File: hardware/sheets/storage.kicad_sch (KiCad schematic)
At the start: 32 parts, among them J1 Conn_02x20_Odd_Even, J2 Conn_02x25_Odd_Even, Q1 2N7002, U1 74HC04, U10 74LVC573A, U11 74HC138, U2 74HC08, U3 74HC08, U4 74HC32, U5 74LVC125A, U6 74HC138, U7 74HC138, U8 74LVC245A, U9 74LVC573A

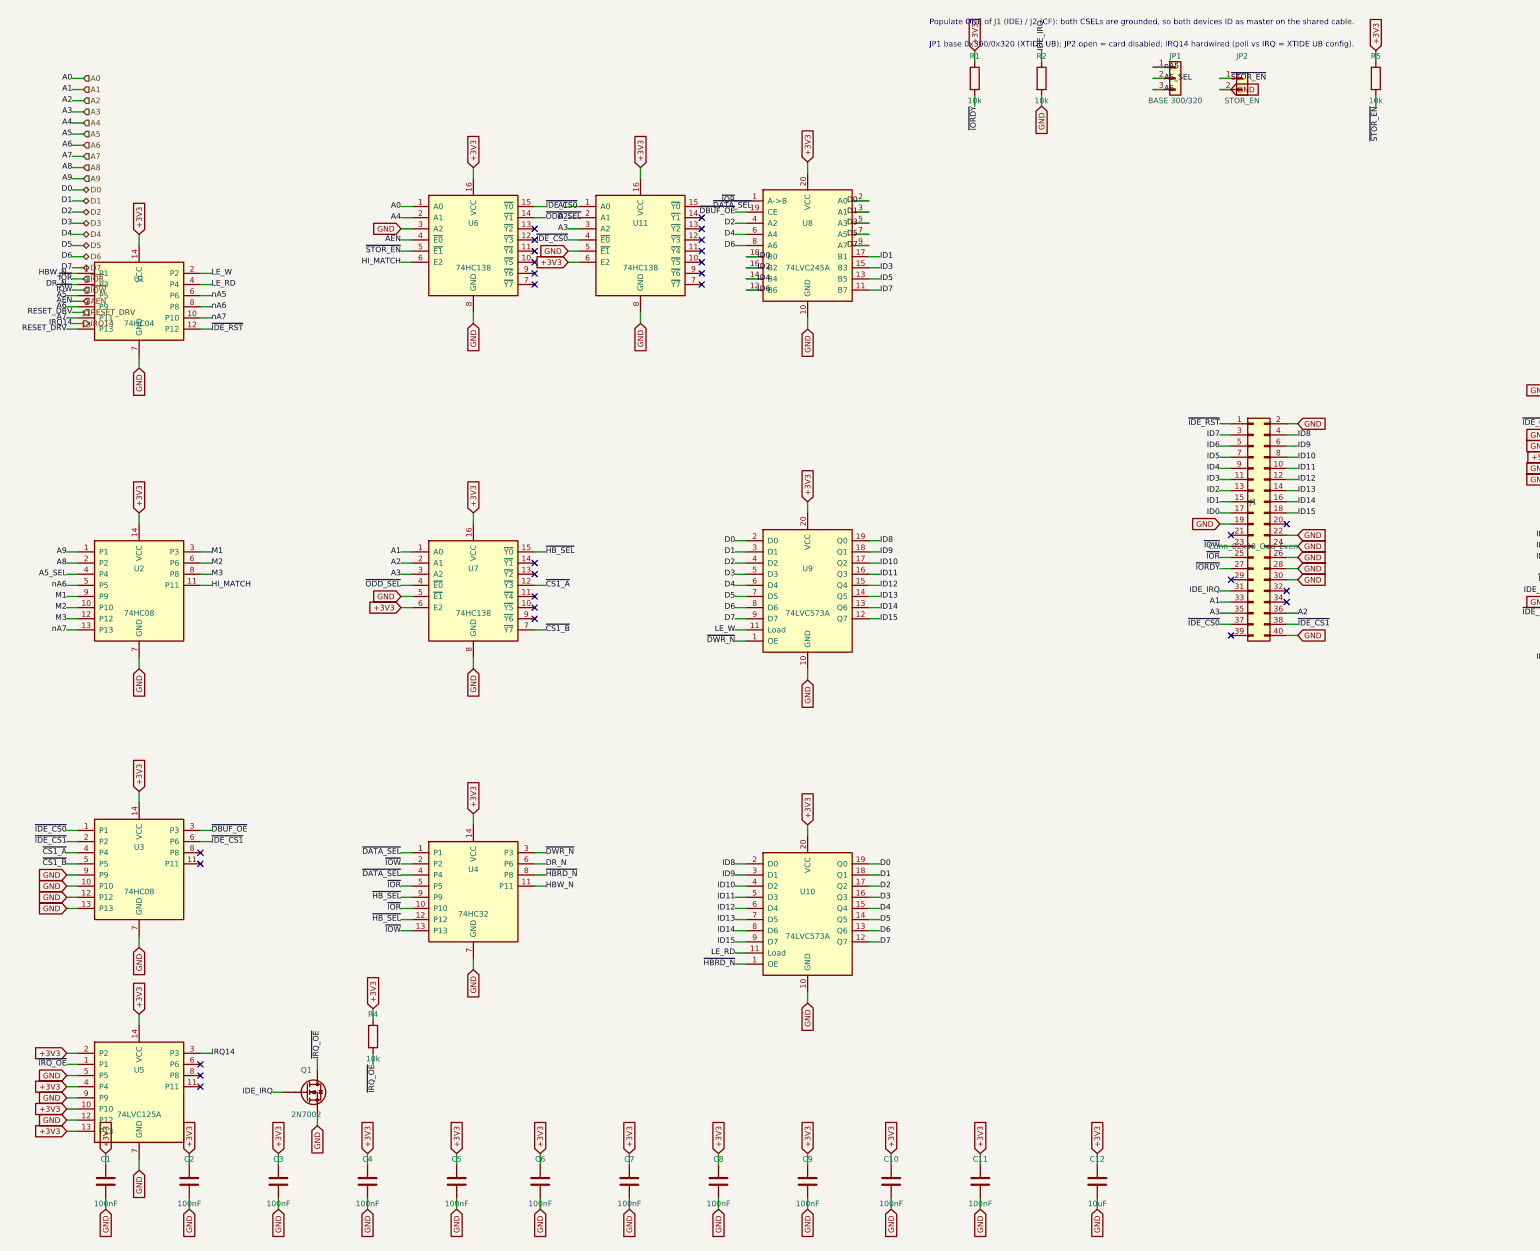
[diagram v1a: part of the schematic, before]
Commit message: addr_decode: central I/O decode, IRQ mapping + disable jumpers; UART -> TL16C550CPFBR
New addr_decode sheet owns the discrete peripherals' bus plumbing:
'138+'00+'32 windowed decode exports ~COM1/~COM2/~LPT/~IDE chip selects
(0x3F8/0x2F8/0x378 share one A5.A4.A3 fine term); one shared 74LVC125A
maps the peripherals' private IRQ requests onto IRQ4/3/7/14 (COM keeps
~OUT2 gating), replacing the three per-sheet '125s; base straps (JP1/JP2,
pulled-high commons) and per-peripheral disable jumpers JP3-JP6 (enabled
by default, fit to disable via a second '32 rank on the CS) live here.
com_port/parallel/storage lose their decode gates, IRQ drivers and
enable jumpers; board drops 97 -> 93 ICs. Docs reframed per feedback:
PRIV_CS/PRIV_IRQREQ are shared logic factored out, not isolation breaks.

UART rebound to the active TL16C550CPFBR (TQFP-48, LCSC C882798, thin
stock) -- pinout verified identical to the symbol via jlc_get_pinout;
parts.py-only swap, sourcing notes updated.

Co-Authored-By: Claude Fable 5 <noreply@anthropic.com>
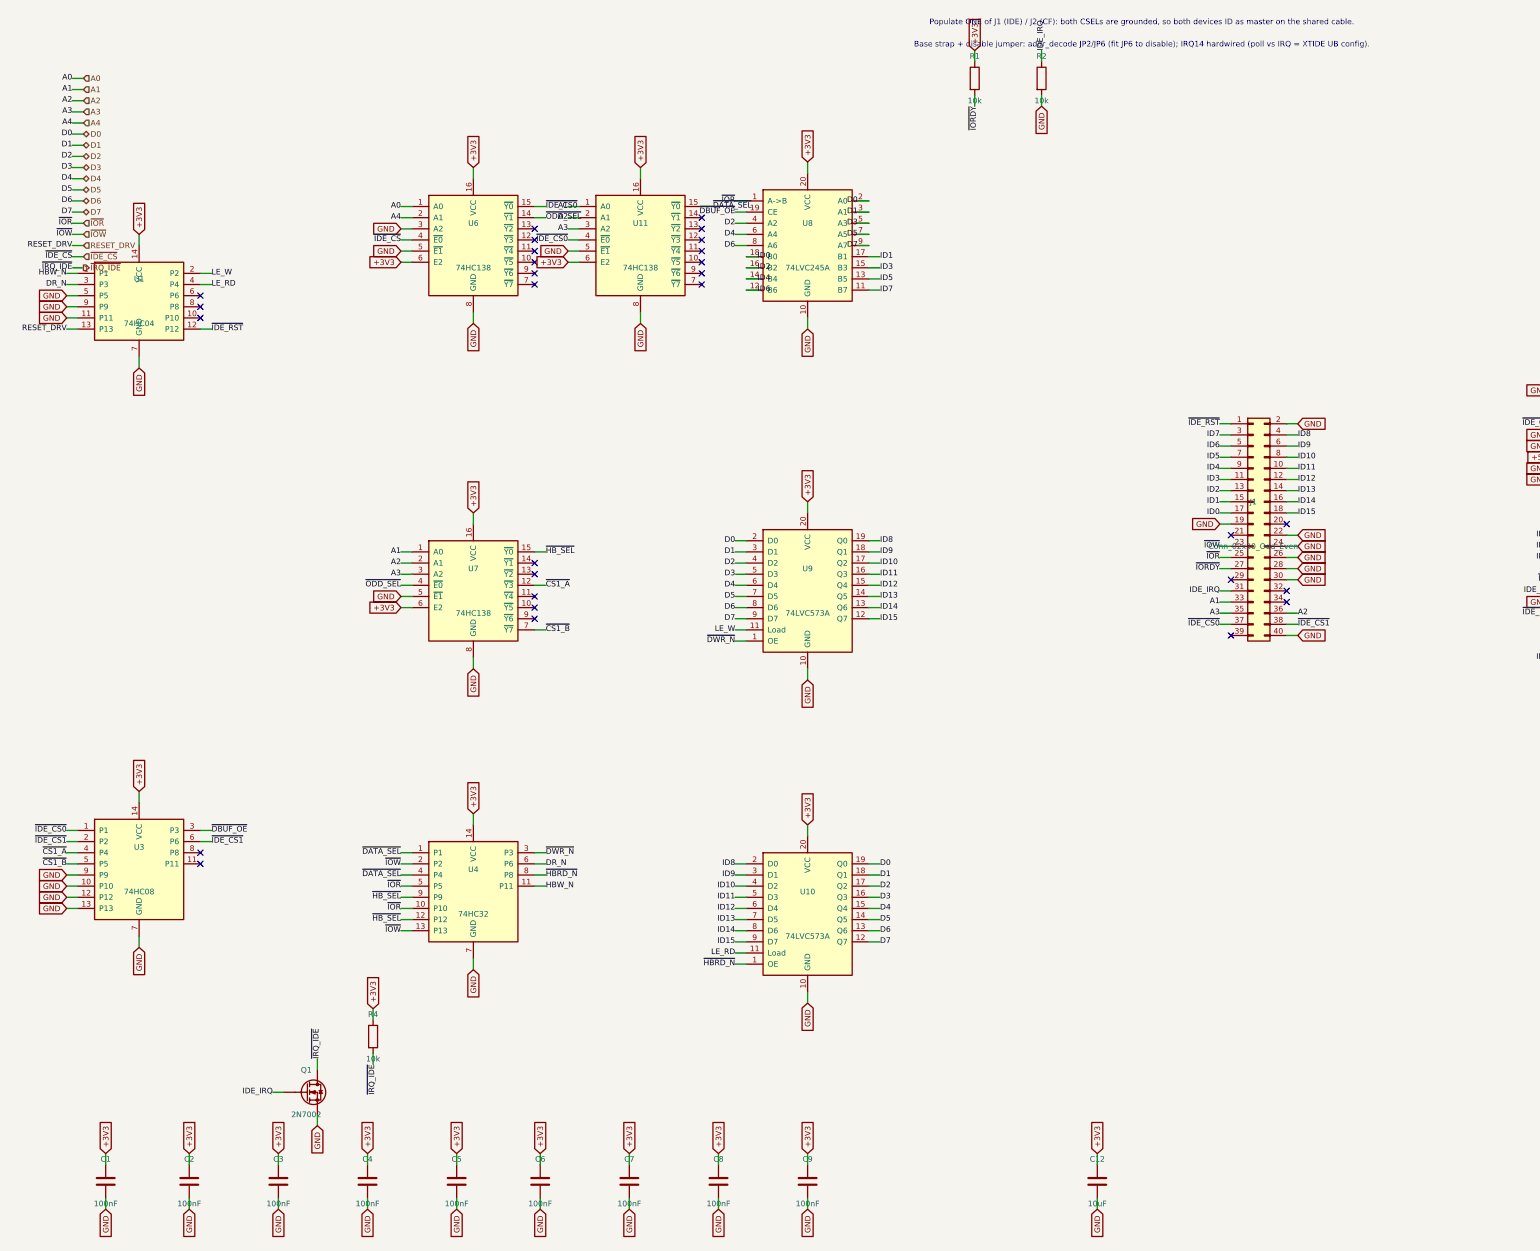
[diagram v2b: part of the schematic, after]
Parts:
- removed C10, C11: 100nF, Capacitor_SMD:C_0603_1608Metric, symbol Device:C
- removed JP1: BASE 300/320, Connector_PinHeader_2.54mm:PinHeader_1x03_P2.54mm_Vertical, symbol Connector_Generic:Conn_01x03
- removed JP2: STOR_EN, Connector_PinHeader_2.54mm:PinHeader_1x02_P2.54mm_Vertical, symbol Connector_Generic:Conn_01x02
- removed R5: 10k, Resistor_SMD:R_0603_1608Metric, symbol Device:R
- removed U2: 74HC08, Package_SO:SOIC-14_3.9x8.7mm_P1.27mm, symbol mini-xt:74HCT08
- removed U5: 74LVC125A, Package_SO:SOIC-14_3.9x8.7mm_P1.27mm, symbol mini-xt:74HCT125
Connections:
- net A5 is gone; now on net GND: U1.5 (P5)
- net A6 is gone; now on net GND: U1.9 (P9)
- net A7 is gone; now on net GND: U1.11 (P11)
- net HI_MATCH is gone; now on net +3V3: U6.6 (E2)
- net ~{STOR_EN} is gone; now on net GND: U6.5 (~{E1})
- net AEN renamed ~{IDE_CS}
- net nA5: no longer names the net of U1.6 (P6)
- net nA6: no longer names the net of U1.8 (P8)
- net nA7: no longer names the net of U1.10 (P10)
- net ~{IRQ_OE} renamed ~{IRQ_IDE}
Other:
- note added: "Base strap + disable jumper: addr_decode JP2/JP6 (fit JP6 to disable); IRQ14 hardwired (poll vs IRQ = XTIDE UB config)."
- note removed: "JP1 base 0x300/0x320 (XTIDE UB); JP2 open = card disabled; IRQ14 hardwired (poll vs IRQ = XTIDE UB config)."

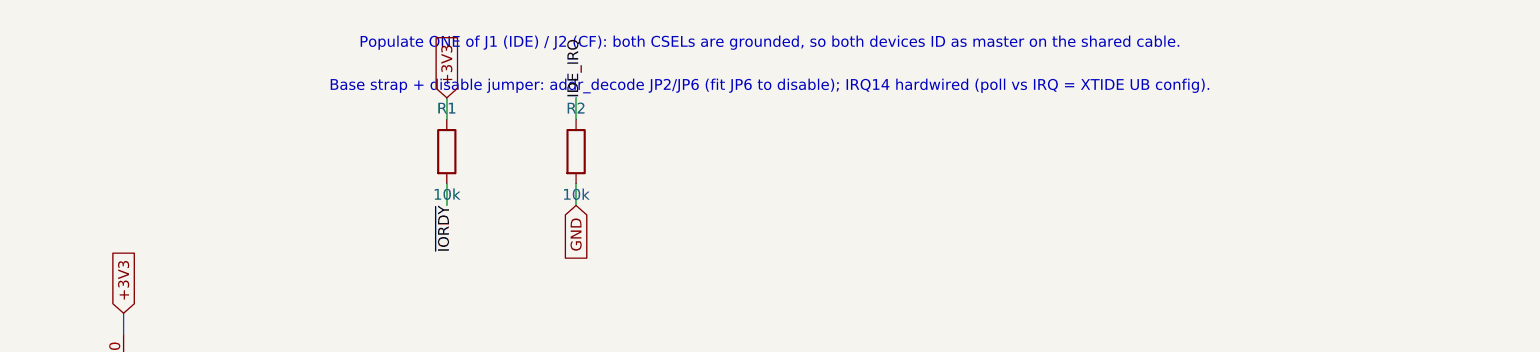
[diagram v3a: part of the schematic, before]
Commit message: bus_mcu: delete U17 (74LVC04A, 1/6 gates) -- HLDA inverter moves to parallel's spare gate
The HLDA -> ~{HLDA} inversion for the counter '244s now lives on the
parallel sheet's spare 74AHC14 Schmitt gate (U9.1, freed by the decode
centralization) -- the board's only spare 5V-tolerant inverter, which is
what HLDA (raw 5V V20 output) requires. ~{HLDA} joins mxbus.PRIV_CPU and
crosses as an interface net; park-safety unchanged (R18 parks HLDA low,
~{HLDA} idles high, '244s off during MCU-Hi-Z). U17 + its decoupler
deleted; the orphaned 74LVC04A parts.py line (C282341) removed. Board
454 comps / 92 ICs. Also sweeps stale JP-number refs left in the
parallel/storage/com_port docstrings from the jumper renumber.

Co-Authored-By: Claude Fable 5 <noreply@anthropic.com>
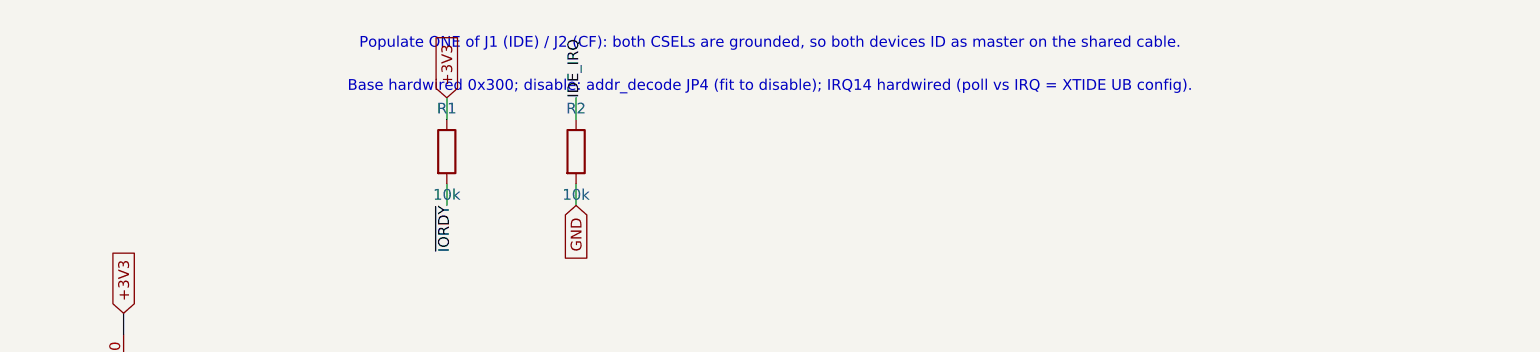
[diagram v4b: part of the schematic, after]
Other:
- note added: "Base hardwired 0x300; disable: addr_decode JP4 (fit to disable); IRQ14 hardwired (poll vs IRQ = XTIDE UB config)."
- note removed: "Base strap + disable jumper: addr_decode JP2/JP6 (fit JP6 to disable); IRQ14 hardwired (poll vs IRQ = XTIDE UB config)."
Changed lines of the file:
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@@
 		)
 	)
-	(text "Base strap + disable jumper: addr_decode JP2/JP6 (fit JP6 to disable); IRQ14 hardwired (poll vs IRQ = XTIDE UB config)."
+	(text "Base hardwired 0x300; disable: addr_decode JP4 (fit to disable); IRQ14 hardwired (poll vs IRQ = XTIDE UB config)."
 		(at 266.7 17.78 0)
 		(effects
@@
 		(instances
 			(project "mini-xt"
-				(path "/26736c46-8b40-5460-874f-03596d17270c/0764659c-2e18-5233-8e35-52713602aecc"
+				(path "/26736c46-8b40-5460-874f-03596d17270c/3d789b7e-8571-58c2-8404-2016fa912ed0"
 					(reference "U801")
 					(unit 1)
@@
 		(instances
 			(project "mini-xt"
-				(path "/26736c46-8b40-5460-874f-03596d17270c/0764659c-2e18-5233-8e35-52713602aecc"
+				(path "/26736c46-8b40-5460-874f-03596d17270c/3d789b7e-8571-58c2-8404-2016fa912ed0"
 					(reference "U803")
 					(unit 1)
@@
 		(instances
 			(project "mini-xt"
-				(path "/26736c46-8b40-5460-874f-03596d17270c/0764659c-2e18-5233-8e35-52713602aecc"
+				(path "/26736c46-8b40-5460-874f-03596d17270c/3d789b7e-8571-58c2-8404-2016fa912ed0"
 					(reference "U804")
 					(unit 1)
@@
 		(instances
 			(project "mini-xt"
-				(path "/26736c46-8b40-5460-874f-03596d17270c/0764659c-2e18-5233-8e35-52713602aecc"
+				(path "/26736c46-8b40-5460-874f-03596d17270c/3d789b7e-8571-58c2-8404-2016fa912ed0"
 					(reference "Q801")
 					(unit 1)
@@
 		(instances
 			(project "mini-xt"
-				(path "/26736c46-8b40-5460-874f-03596d17270c/0764659c-2e18-5233-8e35-52713602aecc"
+				(path "/26736c46-8b40-5460-874f-03596d17270c/3d789b7e-8571-58c2-8404-2016fa912ed0"
 					(reference "U806")
 					(unit 1)
@@
 		(instances
 			(project "mini-xt"
-				(path "/26736c46-8b40-5460-874f-03596d17270c/0764659c-2e18-5233-8e35-52713602aecc"
+				(path "/26736c46-8b40-5460-874f-03596d17270c/3d789b7e-8571-58c2-8404-2016fa912ed0"
 					(reference "U807")
 					(unit 1)
@@
 		(instances
 			(project "mini-xt"
-				(path "/26736c46-8b40-5460-874f-03596d17270c/0764659c-2e18-5233-8e35-52713602aecc"
+				(path "/26736c46-8b40-5460-874f-03596d17270c/3d789b7e-8571-58c2-8404-2016fa912ed0"
 					(reference "U811")
 					(unit 1)
@@
 		(instances
 			(project "mini-xt"
-				(path "/26736c46-8b40-5460-874f-03596d17270c/0764659c-2e18-5233-8e35-52713602aecc"
+				(path "/26736c46-8b40-5460-874f-03596d17270c/3d789b7e-8571-58c2-8404-2016fa912ed0"
 					(reference "U808")
 					(unit 1)
@@
 		(instances
 			(project "mini-xt"
-				(path "/26736c46-8b40-5460-874f-03596d17270c/0764659c-2e18-5233-8e35-52713602aecc"
+				(path "/26736c46-8b40-5460-874f-03596d17270c/3d789b7e-8571-58c2-8404-2016fa912ed0"
 					(reference "U809")
 					(unit 1)
@@
 		(instances
 			(project "mini-xt"
-				(path "/26736c46-8b40-5460-874f-03596d17270c/0764659c-2e18-5233-8e35-52713602aecc"
+				(path "/26736c46-8b40-5460-874f-03596d17270c/3d789b7e-8571-58c2-8404-2016fa912ed0"
 					(reference "U810")
 					(unit 1)
@@
 		(instances
 			(project "mini-xt"
-				(path "/26736c46-8b40-5460-874f-03596d17270c/0764659c-2e18-5233-8e35-52713602aecc"
+				(path "/26736c46-8b40-5460-874f-03596d17270c/3d789b7e-8571-58c2-8404-2016fa912ed0"
 					(reference "J801")
 					(unit 1)
@@
 		(instances
 			(project "mini-xt"
-				(path "/26736c46-8b40-5460-874f-03596d17270c/0764659c-2e18-5233-8e35-52713602aecc"
+				(path "/26736c46-8b40-5460-874f-03596d17270c/3d789b7e-8571-58c2-8404-2016fa912ed0"
 					(reference "J802")
 					(unit 1)
@@
 		(instances
 			(project "mini-xt"
-				(path "/26736c46-8b40-5460-874f-03596d17270c/0764659c-2e18-5233-8e35-52713602aecc"
+				(path "/26736c46-8b40-5460-874f-03596d17270c/3d789b7e-8571-58c2-8404-2016fa912ed0"
 					(reference "R801")
 					(unit 1)
@@
 		(instances
 			(project "mini-xt"
-				(path "/26736c46-8b40-5460-874f-03596d17270c/0764659c-2e18-5233-8e35-52713602aecc"
+				(path "/26736c46-8b40-5460-874f-03596d17270c/3d789b7e-8571-58c2-8404-2016fa912ed0"
 					(reference "R802")
 					(unit 1)
@@
 		(instances
 			(project "mini-xt"
-				(path "/26736c46-8b40-5460-874f-03596d17270c/0764659c-2e18-5233-8e35-52713602aecc"
+				(path "/26736c46-8b40-5460-874f-03596d17270c/3d789b7e-8571-58c2-8404-2016fa912ed0"
 					(reference "R804")
 					(unit 1)
@@
 		(instances
 			(project "mini-xt"
-				(path "/26736c46-8b40-5460-874f-03596d17270c/0764659c-2e18-5233-8e35-52713602aecc"
+				(path "/26736c46-8b40-5460-874f-03596d17270c/3d789b7e-8571-58c2-8404-2016fa912ed0"
 					(reference "C801")
 					(unit 1)
@@
 		(instances
 			(project "mini-xt"
-				(path "/26736c46-8b40-5460-874f-03596d17270c/0764659c-2e18-5233-8e35-52713602aecc"
+				(path "/26736c46-8b40-5460-874f-03596d17270c/3d789b7e-8571-58c2-8404-2016fa912ed0"
 					(reference "C802")
 					(unit 1)
@@
 		(instances
 			(project "mini-xt"
-				(path "/26736c46-8b40-5460-874f-03596d17270c/0764659c-2e18-5233-8e35-52713602aecc"
+				(path "/26736c46-8b40-5460-874f-03596d17270c/3d789b7e-8571-58c2-8404-2016fa912ed0"
 					(reference "C803")
 					(unit 1)
@@
 		(instances
 			(project "mini-xt"
-				(path "/26736c46-8b40-5460-874f-03596d17270c/0764659c-2e18-5233-8e35-52713602aecc"
+				(path "/26736c46-8b40-5460-874f-03596d17270c/3d789b7e-8571-58c2-8404-2016fa912ed0"
 					(reference "C804")
 					(unit 1)
@@
 		(instances
 			(project "mini-xt"
-				(path "/26736c46-8b40-5460-874f-03596d17270c/0764659c-2e18-5233-8e35-52713602aecc"
+				(path "/26736c46-8b40-5460-874f-03596d17270c/3d789b7e-8571-58c2-8404-2016fa912ed0"
 					(reference "C805")
 					(unit 1)
@@
 		(instances
 			(project "mini-xt"
-				(path "/26736c46-8b40-5460-874f-03596d17270c/0764659c-2e18-5233-8e35-52713602aecc"
+				(path "/26736c46-8b40-5460-874f-03596d17270c/3d789b7e-8571-58c2-8404-2016fa912ed0"
 					(reference "C806")
 					(unit 1)
@@
 		(instances
 			(project "mini-xt"
-				(path "/26736c46-8b40-5460-874f-03596d17270c/0764659c-2e18-5233-8e35-52713602aecc"
+				(path "/26736c46-8b40-5460-874f-03596d17270c/3d789b7e-8571-58c2-8404-2016fa912ed0"
 					(reference "C807")
 					(unit 1)
@@
 		(instances
 			(project "mini-xt"
-				(path "/26736c46-8b40-5460-874f-03596d17270c/0764659c-2e18-5233-8e35-52713602aecc"
+				(path "/26736c46-8b40-5460-874f-03596d17270c/3d789b7e-8571-58c2-8404-2016fa912ed0"
 					(reference "C808")
 					(unit 1)
@@
 		(instances
 			(project "mini-xt"
-				(path "/26736c46-8b40-5460-874f-03596d17270c/0764659c-2e18-5233-8e35-52713602aecc"
+				(path "/26736c46-8b40-5460-874f-03596d17270c/3d789b7e-8571-58c2-8404-2016fa912ed0"
 					(reference "C809")
 					(unit 1)
@@
 		(instances
 			(project "mini-xt"
-				(path "/26736c46-8b40-5460-874f-03596d17270c/0764659c-2e18-5233-8e35-52713602aecc"
+				(path "/26736c46-8b40-5460-874f-03596d17270c/3d789b7e-8571-58c2-8404-2016fa912ed0"
 					(reference "C812")
 					(unit 1)
